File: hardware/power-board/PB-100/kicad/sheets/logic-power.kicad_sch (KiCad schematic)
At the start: 0 parts

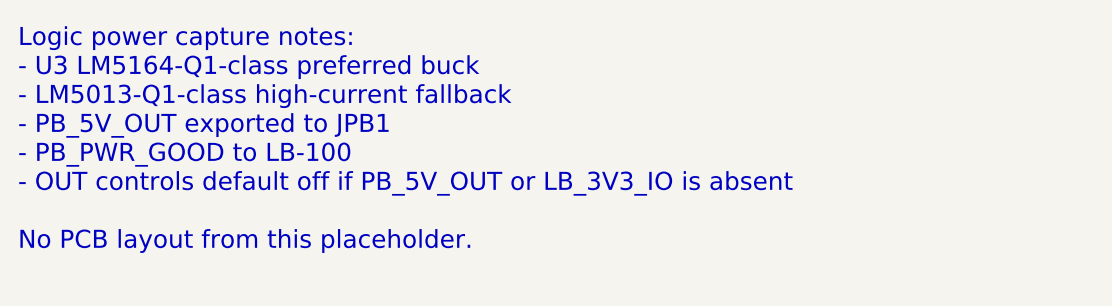
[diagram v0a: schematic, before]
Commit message: hardware: sync pb100 kicad sheet trace notes
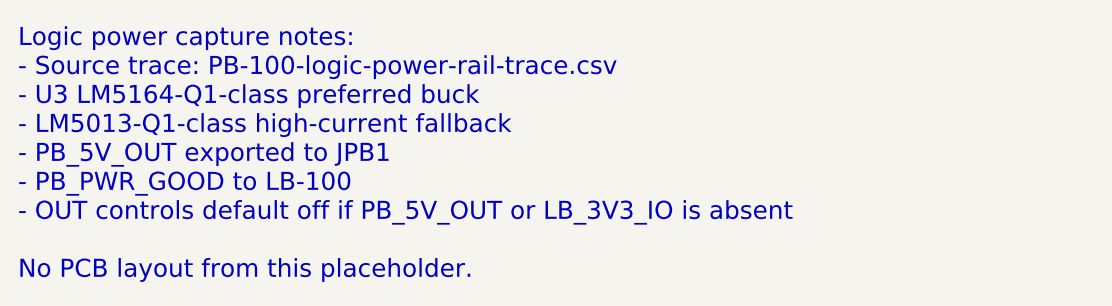
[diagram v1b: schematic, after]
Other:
- note added: "Logic power capture notes: - Source trace: PB-100-logic-power-rail-trace.csv - U3 LM5164-Q1-class preferred buck - LM5013-Q1-class high-current fallback - PB_5V_OUT exported to JPB1 - PB_PWR_GOOD to LB-100 - OUT controls default off if PB_5V_OUT or LB_3V3_IO is absent No PCB layout from this placeholder."
- note removed: "Logic power capture notes: - U3 LM5164-Q1-class preferred buck - LM5013-Q1-class high-current fallback - PB_5V_OUT exported to JPB1 - PB_PWR_GOOD to LB-100 - OUT controls default off if PB_5V_OUT or LB_3V3_IO is absent No PCB layout from this placeholder."
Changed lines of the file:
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@@
     (comment 9 "Work queue: CAP-LOGIC. Logic power capture follows buck pin template and design values.")
     (comment 1 "Placeholder sheet. Capture PB_5V_OUT buck regulator and power-good here.")
-    (comment 2 "Source docs: PB-100-logic-power-rails.md and PB-100-logic-power-budget.csv.")
+    (comment 2 "Sources: PB-100-logic-power-rail-trace.csv, PB-100-logic-power-design-values.csv, PB-100-logic-power-budget.csv.")
   )
-  (text "Logic power capture notes:\n- U3 LM5164-Q1-class preferred buck\n- LM5013-Q1-class high-current fallback\n- PB_5V_OUT exported to JPB1\n- PB_PWR_GOOD to LB-100\n- OUT controls default off if PB_5V_OUT or LB_3V3_IO is absent\n\nNo PCB layout from this placeholder."
+  (text "Logic power capture notes:\n- Source trace: PB-100-logic-power-rail-trace.csv\n- U3 LM5164-Q1-class preferred buck\n- LM5013-Q1-class high-current fallback\n- PB_5V_OUT exported to JPB1\n- PB_PWR_GOOD to LB-100\n- OUT controls default off if PB_5V_OUT or LB_3V3_IO is absent\n\nNo PCB layout from this placeholder."
     (at 25 30 0)
     (effects (font (size 2.0 2.0)) (justify left top))

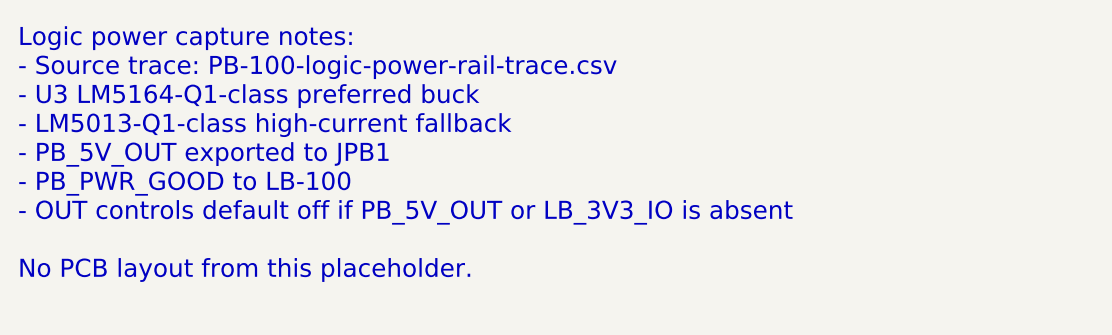
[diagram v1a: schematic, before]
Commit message: hardware: add pb100 logic power freeze review
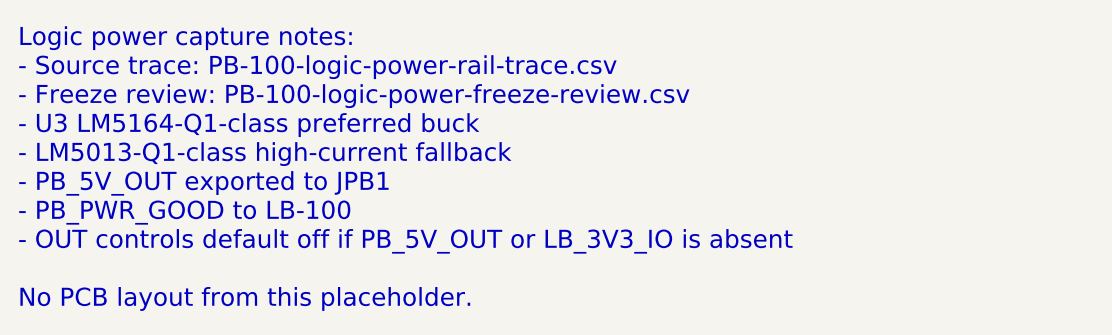
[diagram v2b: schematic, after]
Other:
- note added: "Logic power capture notes: - Source trace: PB-100-logic-power-rail-trace.csv - Freeze review: PB-100-logic-power-freeze-review.csv - U3 LM5164-Q1-class preferred buck - LM5013-Q1-class high-current fallback - PB_5V_OUT exported to JPB1 - PB_PWR_GOOD to LB-100 - OUT controls default off if PB_5V_OUT or LB_3V3_IO is absent No PCB layout from this placeholder."
- note removed: "Logic power capture notes: - Source trace: PB-100-logic-power-rail-trace.csv - U3 LM5164-Q1-class preferred buck - LM5013-Q1-class high-current fallback - PB_5V_OUT exported to JPB1 - PB_PWR_GOOD to LB-100 - OUT controls default off if PB_5V_OUT or LB_3V3_IO is absent No PCB layout from this placeholder."
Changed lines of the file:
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@@
     (comment 9 "Work queue: CAP-LOGIC. Logic power capture follows buck pin template and design values.")
     (comment 1 "Placeholder sheet. Capture PB_5V_OUT buck regulator and power-good here.")
-    (comment 2 "Sources: PB-100-logic-power-rail-trace.csv, PB-100-logic-power-design-values.csv, PB-100-logic-power-budget.csv.")
+    (comment 2 "Sources: PB-100-logic-power-rail-trace.csv, PB-100-logic-power-freeze-review.csv, PB-100-logic-power-design-values.csv, PB-100-logic-power-budget.csv.")
   )
-  (text "Logic power capture notes:\n- Source trace: PB-100-logic-power-rail-trace.csv\n- U3 LM5164-Q1-class preferred buck\n- LM5013-Q1-class high-current fallback\n- PB_5V_OUT exported to JPB1\n- PB_PWR_GOOD to LB-100\n- OUT controls default off if PB_5V_OUT or LB_3V3_IO is absent\n\nNo PCB layout from this placeholder."
+  (text "Logic power capture notes:\n- Source trace: PB-100-logic-power-rail-trace.csv\n- Freeze review: PB-100-logic-power-freeze-review.csv\n- U3 LM5164-Q1-class preferred buck\n- LM5013-Q1-class high-current fallback\n- PB_5V_OUT exported to JPB1\n- PB_PWR_GOOD to LB-100\n- OUT controls default off if PB_5V_OUT or LB_3V3_IO is absent\n\nNo PCB layout from this placeholder."
     (at 25 30 0)
     (effects (font (size 2.0 2.0)) (justify left top))

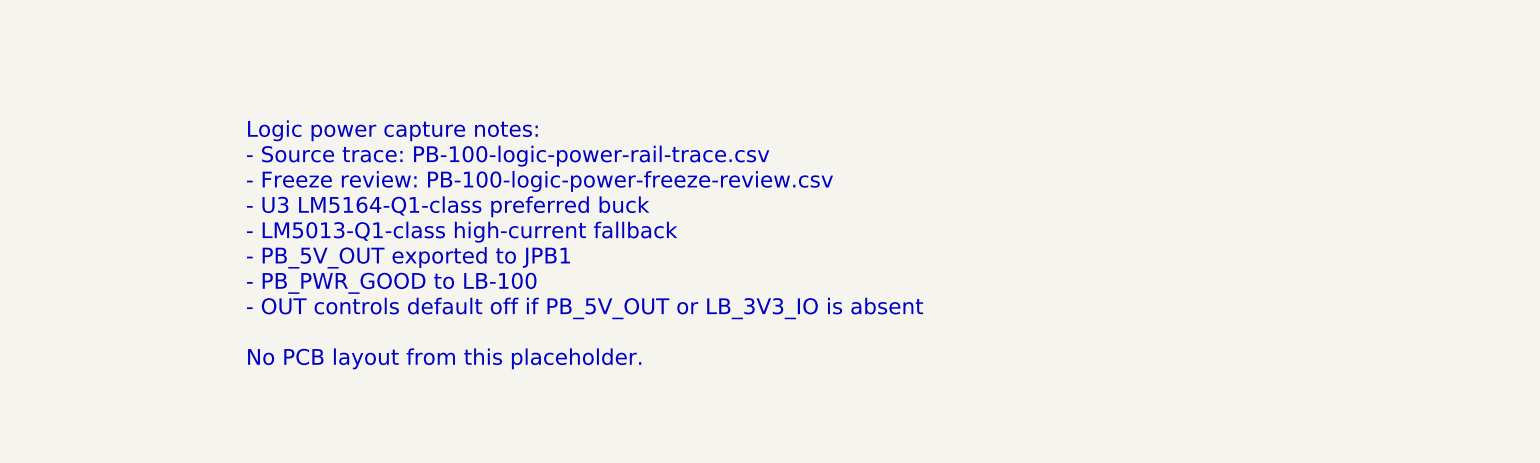
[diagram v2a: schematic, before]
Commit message: Capture preliminary PB-100 schematic sheets
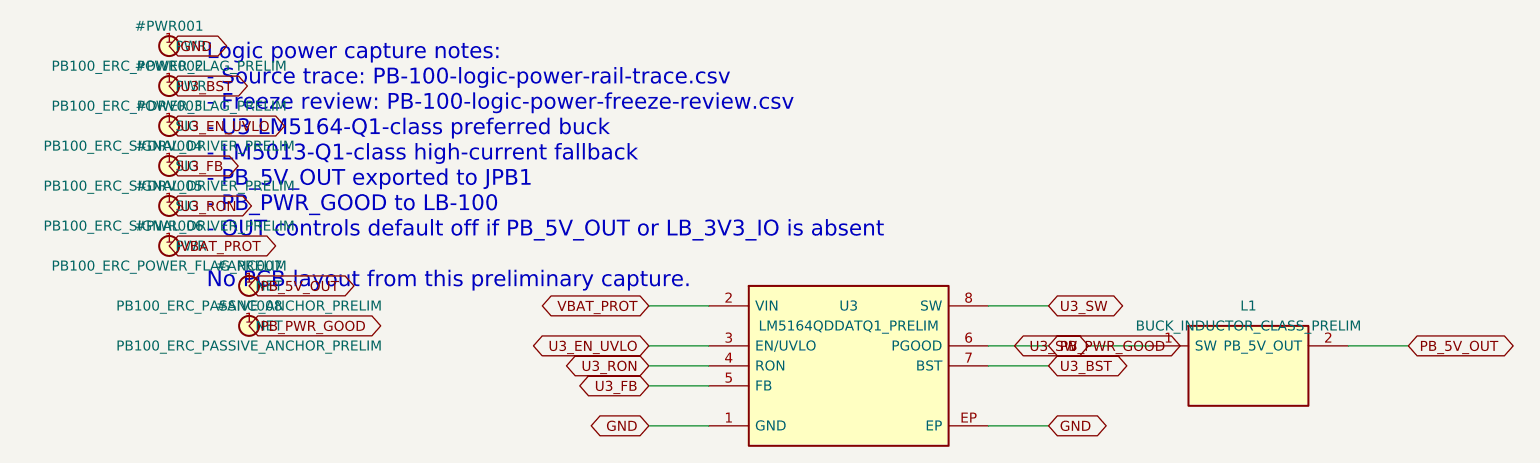
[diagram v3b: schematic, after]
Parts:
- added L1: BUCK_INDUCTOR_CLASS_PRELIM, symbol PB100:PB100_BUCK_INDUCTOR_CLASS_PRELIM
- added U3: LM5164QDDATQ1_PRELIM, symbol PB100:PB100_LM5164QDDATQ1_PRELIM
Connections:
- new net GND: U3.1 (GND), U3.EP
- new net PB_5V_OUT: L1.2 (PB_5V_OUT)
- new net PB_PWR_GOOD: U3.6 (PGOOD)
- new net U3_BST: U3.7 (BST)
- new net U3_EN_UVLO: U3.3 (EN/UVLO)
- new net U3_FB: U3.5 (FB)
- new net U3_RON: U3.4 (RON)
- new net U3_SW: L1.1 (SW), U3.8 (SW)
- new net VBAT_PROT: U3.2 (VIN)
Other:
- note added: "Logic power capture notes: - Source trace: PB-100-logic-power-rail-trace.csv - Freeze review: PB-100-logic-power-freeze-review.csv - U3 LM5164-Q1-class preferred buck - LM5013-Q1-class high-current fallback - PB_5V_OUT exported to JPB1 - PB_PWR_GOOD to LB-100 - OUT controls default off if PB_5V_OUT or LB_3V3_IO is absent No PCB layout from this preliminary capture."
- note removed: "Logic power capture notes: - Source trace: PB-100-logic-power-rail-trace.csv - Freeze review: PB-100-logic-power-freeze-review.csv - U3 LM5164-Q1-class preferred buck - LM5013-Q1-class high-current fallback - PB_5V_OUT exported to JPB1 - PB_PWR_GOOD to LB-100 - OUT controls default off if PB_5V_OUT or LB_3V3_IO is absent No PCB layout from this placeholder."

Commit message: Add PB-100 logic power freeze checklist
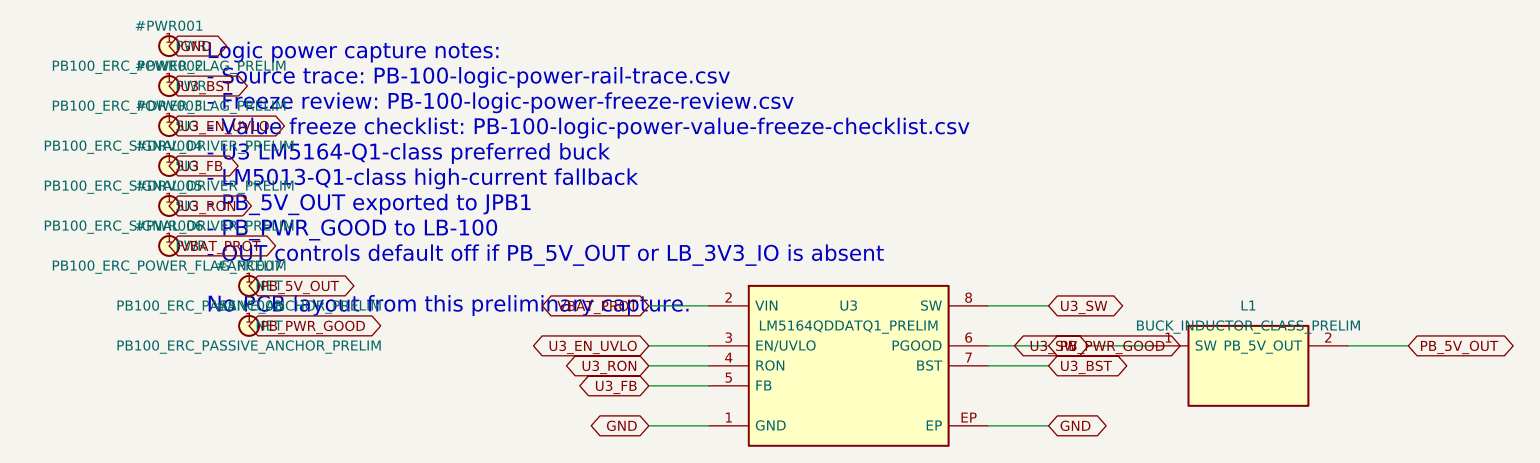
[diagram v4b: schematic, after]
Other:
- note added: "Logic power capture notes: - Source trace: PB-100-logic-power-rail-trace.csv - Freeze review: PB-100-logic-power-freeze-review.csv - Value freeze checklist: PB-100-logic-power-value-freeze-checklist.csv - U3 LM5164-Q1-class preferred buck - LM5013-Q1-class high-current fallback - PB_5V_OUT exported to JPB1 - PB_PWR_GOOD to LB-100 - OUT controls default off if PB_5V_OUT or LB_3V3_IO is absent No P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"
- note removed: "Logic power capture notes: - Source trace: PB-100-logic-power-rail-trace.csv - Freeze review: PB-100-logic-power-freeze-review.csv - U3 LM5164-Q1-class preferred buck - LM5013-Q1-class high-current fallback - PB_5V_OUT exported to JPB1 - PB_PWR_GOOD to LB-100 - OUT controls default off if PB_5V_OUT or LB_3V3_IO is absent No PCB layout from this preliminary capture."
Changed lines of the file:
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@@
     (comment 9 "Work queue: CAP-LOGIC. Preliminary schematic capture follows PB-100-schematic-capture-work-queue.csv.")
     (comment 1 "Preliminary capture for PB_5V_OUT buck regulator and power-good.")
-    (comment 2 "Sources: PB-100-logic-power-rail-trace.csv, PB-100-logic-power-freeze-review.csv, PB-100-logic-power-design-values.csv, PB-100-logic-power-budget.csv.")
+    (comment 2 "Sources: PB-100-logic-power-rail-trace.csv, PB-100-logic-power-freeze-review.csv, PB-100-logic-power-value-freeze-checklist.csv, PB-100-logic-power-design-values.csv, PB-100-logic-power-budget.csv.")
   )
-  (text "Logic power capture notes:\n- Source trace: PB-100-logic-power-rail-trace.csv\n- Freeze review: PB-100-logic-power-freeze-review.csv\n- U3 LM5164-Q1-class preferred buck\n- LM5013-Q1-class high-current fallback\n- PB_5V_OUT exported to JPB1\n- PB_PWR_GOOD to LB-100\n- OUT controls default off if PB_5V_OUT or LB_3V3_IO is absent\n\nNo PCB layout from this preliminary capture."
+  (text "Logic power capture notes:\n- Source trace: PB-100-logic-power-rail-trace.csv\n- Freeze review: PB-100-logic-power-freeze-review.csv\n- Value freeze checklist: PB-100-logic-power-value-freeze-checklist.csv\n- U3 LM5164-Q1-class preferred buck\n- LM5013-Q1-class high-current fallback\n- PB_5V_OUT exported to JPB1\n- PB_PWR_GOOD to LB-100\n- OUT controls default off if PB_5V_OUT or LB_3V3_IO is absent\n\nNo PCB layout from this preliminary capture."
     (at 20 20 0)
     (effects (font (size 2.0 2.0)) (justify left top))
